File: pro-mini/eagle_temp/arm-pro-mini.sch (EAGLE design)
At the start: 61 parts, among them J1 MICRO USB, J2 SWD HEADER, Q1 12Mhz, T1 MMBT3906, U1 PRTR5V0U2X, U2 MIC5225-3.3v, U3 LPC11U35FHI33/501, U4 BAS40-05

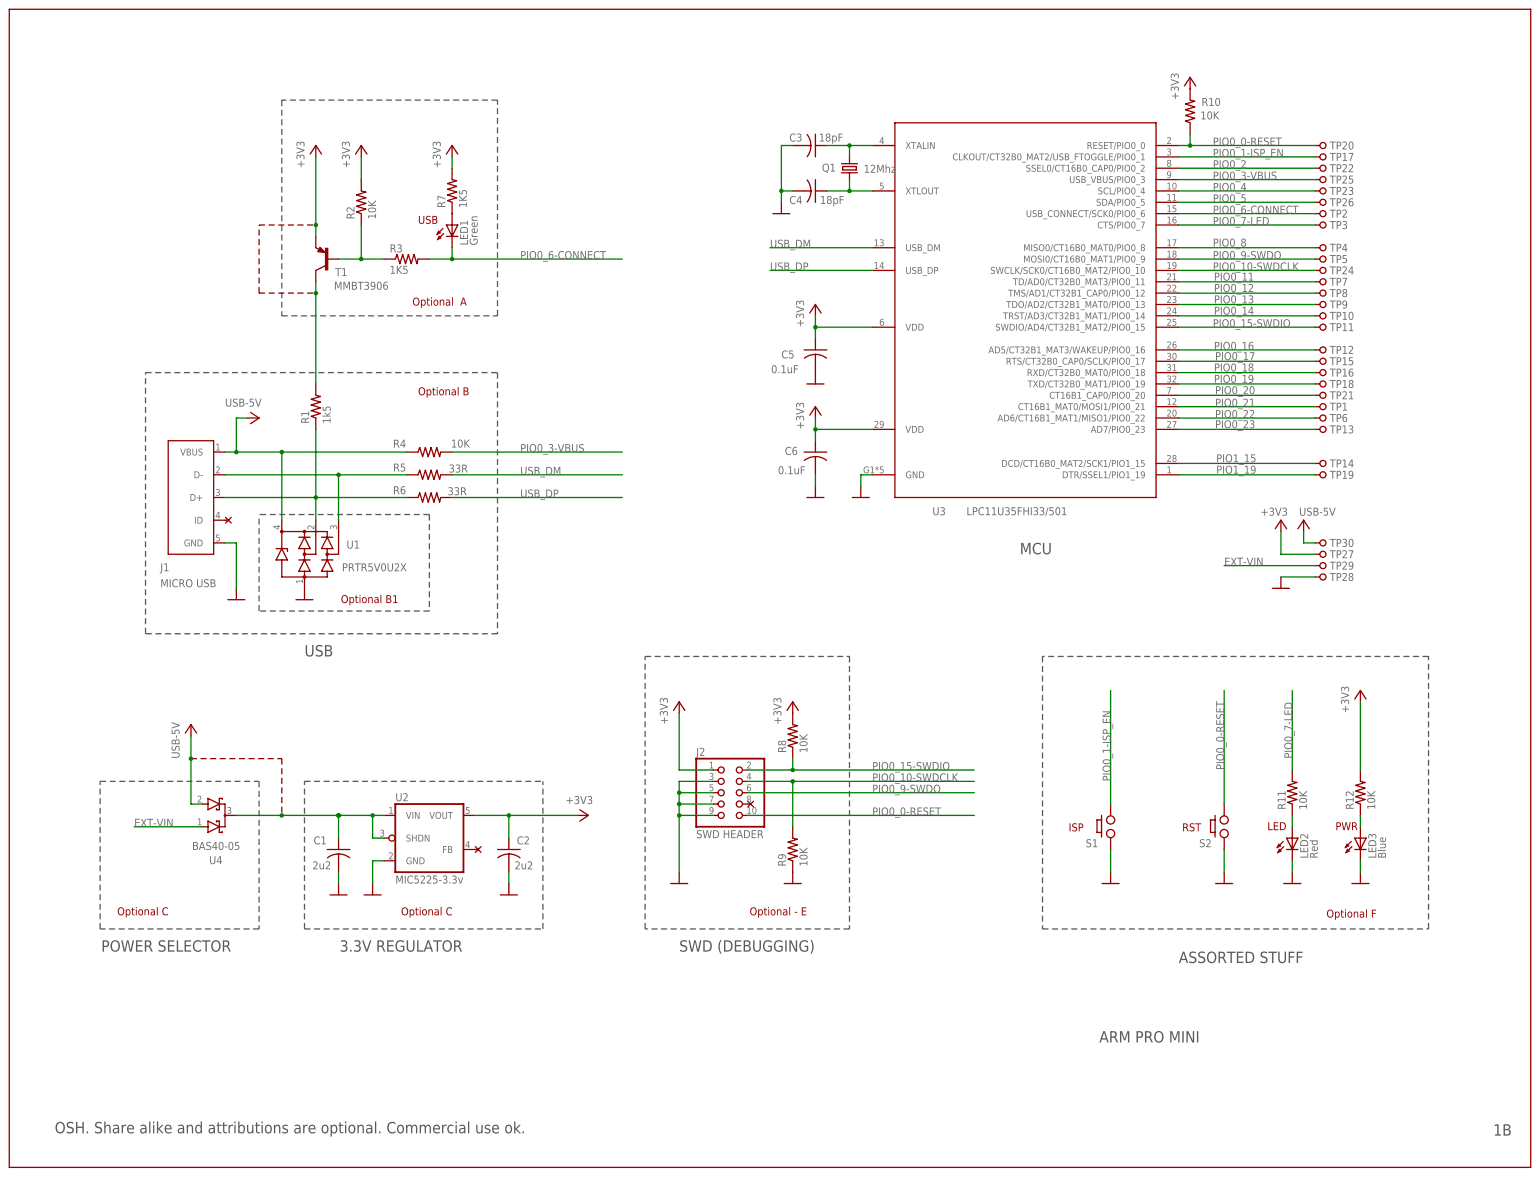
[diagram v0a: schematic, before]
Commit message: Work in progress. Layout auto routs 100%. Requires net list and footprints verification.
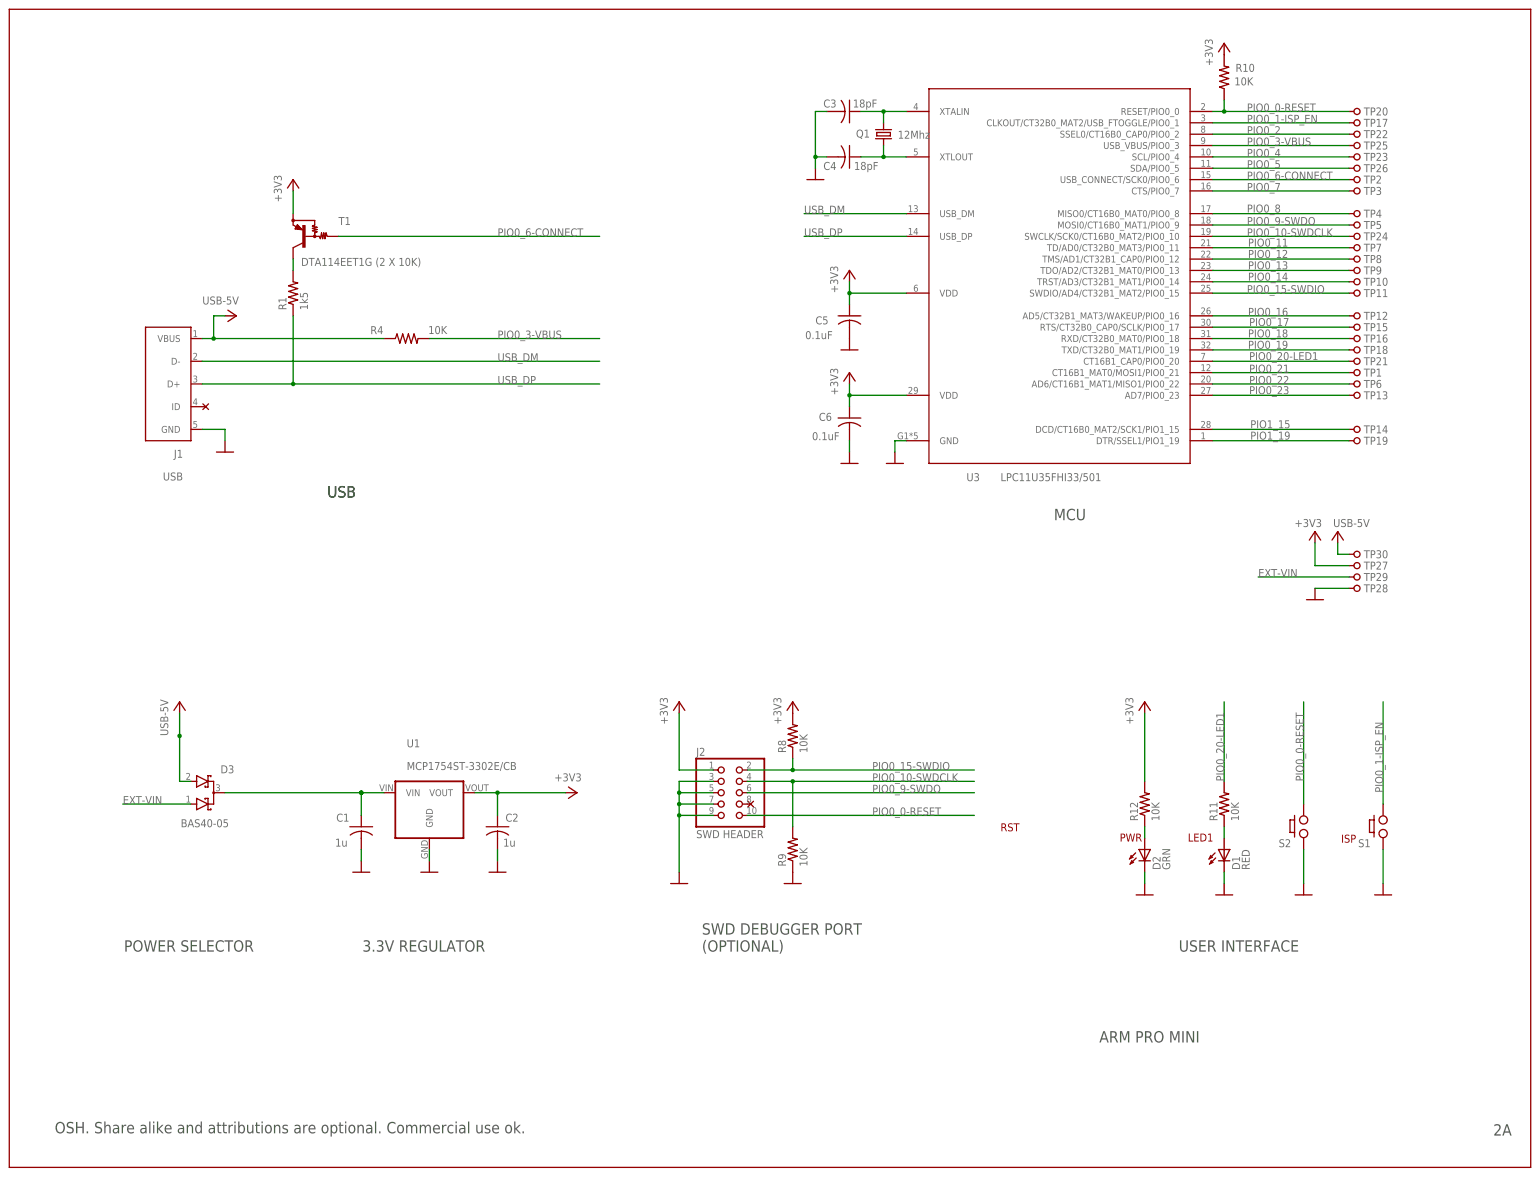
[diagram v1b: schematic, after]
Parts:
- removed LED1: Green, arm-pro-mini:LEDCHIP-LED0603
- removed LED2: Red, arm-pro-mini:LEDCHIP-LED0603
- removed LED3: Blue, arm-pro-mini:LEDCHIP-LED0603
- removed R2: 10K, arm-pro-mini:R-US_R0402
- removed R3, R7: 1K5, arm-pro-mini:R-US_R0402
- removed R5, R6: 33R, arm-pro-mini:R-US_R0402
- removed U2: MIC5225-3.3v, arm-pro-mini:TC1015
- removed U4: BAS40-05, arm-pro-mini:BAS40-05
- added D1: RED, arm-pro-mini:LED
- added D2: GRN, arm-pro-mini:LED
- added D3: BAS40-05, arm-pro-mini:BAS40-05
- C1, C2: value 2u2 -> 1u
- J1: value MICRO USB -> USB
- T1: value MMBT3906 -> DTA114EET1G (2 X 10K); device arm-pro-mini:BC857B-PNP-SOT23-BEC -> arm-pro-mini:PNP_RESISTORS
- U1: value PRTR5V0U2X -> MCP1754ST-3302E/CB; device arm-pro-mini:PRTR5V0U2X -> arm-pro-mini:LDO
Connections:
- removed net N$4: R2.1, R3.1, T1.B
- removed net N$7: LED1.A, R7.1
- removed net N$8: J1.D+, R1.1, R6.1, U1.IO1
- removed net N$9: J1.D-, R5.1, U1.IO2
- removed net PIO0_20: TP21.1, U3.CT16B1_CAP0/PIO0_20
- removed net PIO0_7-LED: R11.2, TP3.1, U3.CTS/PIO0_7
- new net PIO0_20-LED1: R11.2, TP21.1, U3.CT16B1_CAP0/PIO0_20
- new net PIO0_7: TP3.1, U3.CTS/PIO0_7
- net +3V3: now also U1.VOUT; no longer R2.2, R7.2, U2.VOUT
- net EXT-VIN: now also D3.A1; no longer U4.A1
- net GND: now also D1.C, D2.C; no longer LED2.C, LED3.C, U2.GND
- net N$10: now also D3.C, U1.VIN; no longer U2.SHDN, U2.VIN, U4.C
- net N$2: now also D2.A; no longer LED3.A
- net N$6: now also D1.A; no longer LED2.A
- net PIO0_6-CONNECT: now also T1.B; no longer LED1.C, R3.2
- net USB-5V: now also D3.A2; no longer U1.VCC, U4.A2
- net USB_DM: now also J1.D-; no longer R5.2
- net USB_DP: now also J1.D+, R1.1; no longer R6.2
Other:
- note added: "2A"
- note added: "LED1"
- note added: "SWD DEBUGGER PORT (OPTIONAL)"
- note added: "USER INTERFACE"
- note removed: "1B"
- note removed: "ASSORTED STUFF"
- note removed: "LED"
- note removed: "Optional - E"
- note removed: "Optional A"
- note removed: "Optional B"
- note removed: "Optional B1"
- note removed: "Optional C"
- note removed: "Optional F"
- note removed: "SWD (DEBUGGING)"
- moved on the sheet: C1, C2, C3, C4, C5, C6, J1, Q1, R1, R10, R11, R12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

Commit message: Ready for final auto routing.
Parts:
- removed R8: 10K, arm-pro-mini:R-US_R0402
- added R2: 10K, arm-pro-mini:R-US_R0402
- TP1: device arm-pro-mini:PINHD-1X1SQUARE -> arm-pro-mini:PINHD-1X1
- renumbered R10 to R5, R11 to R7, R12 to R6, R9 to R3
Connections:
- net +3V3: now also R4.2; no longer R8.2
- net PIO0_15-SWDIO: now also R4.1; no longer R8.1
- net PIO0_3-VBUS: now also R2.2; no longer R4.2
- net USB-5V: now also R2.1; no longer R4.1
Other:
- moved on the sheet: J1, R4
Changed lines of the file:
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@@
 <part name="+3V6" library="arm-pro-mini" deviceset="+3V3" device=""/>
 <part name="GND12" library="arm-pro-mini" deviceset="GND" device=""/>
-<part name="R8" library="arm-pro-mini" deviceset="R-US_" device="R0402" value="10K"/>
-<part name="R9" library="arm-pro-mini" deviceset="R-US_" device="R0402" value="10K"/>
+<part name="R4" library="arm-pro-mini" deviceset="R-US_" device="R0402" value="10K"/>
+<part name="R3" library="arm-pro-mini" deviceset="R-US_" device="R0402" value="10K"/>
 <part name="GND13" library="arm-pro-mini" deviceset="GND" device=""/>
 <part name="+3V7" library="arm-pro-mini" deviceset="+3V3" device=""/>
-<part name="R10" library="arm-pro-mini" deviceset="R-US_" device="R0402" value="10K"/>
+<part name="R5" library="arm-pro-mini" deviceset="R-US_" device="R0402" value="10K"/>
 <part name="+3V8" library="arm-pro-mini" deviceset="+3V3" device=""/>
 <part name="S2" library="arm-pro-mini" deviceset="PUSH_BUTTON" device=""/>
 <part name="GND14" library="arm-pro-mini" deviceset="GND" device=""/>
-<part name="R4" library="arm-pro-mini" deviceset="R-US_" device="R0402" value="10K"/>
+<part name="R2" library="arm-pro-mini" deviceset="R-US_" device="R0402" value="10K"/>
 <part name="+3V9" library="arm-pro-mini" deviceset="+3V3" device=""/>
-<part name="R12" library="arm-pro-mini" deviceset="R-US_" device="R0402" value="10K"/>
+<part name="R6" library="arm-pro-mini" deviceset="R-US_" device="R0402" value="10K"/>
 <part name="GND5" library="arm-pro-mini" deviceset="GND" device=""/>
-<part name="R11" library="arm-pro-mini" deviceset="R-US_" device="R0402" value="10K"/>
+<part name="R7" library="arm-pro-mini" deviceset="R-US_" device="R0402" value="10K"/>
 <part name="GND6" library="arm-pro-mini" deviceset="GND" device=""/>
 <part name="+3V4" library="arm-pro-mini" deviceset="+3V3" device=""/>
@@
 <part name="TP18" library="arm-pro-mini" deviceset="PINHD-1X1" device="" value="HDR1"/>
 <part name="TP21" library="arm-pro-mini" deviceset="PINHD-1X1" device="" value="HDR1"/>
-<part name="TP1" library="arm-pro-mini" deviceset="PINHD-1X1" device="SQUARE" value="HDR1"/>
+<part name="TP1" library="arm-pro-mini" deviceset="PINHD-1X1" device="" value="HDR1"/>
 <part name="TP6" library="arm-pro-mini" deviceset="PINHD-1X1" device="" value="HDR1"/>
 <part name="TP13" library="arm-pro-mini" deviceset="PINHD-1X1" device="" value="HDR1"/>
@@
 <instance part="+3V6" gate="G$1" x="149.86" y="104.14"/>
 <instance part="GND12" gate="1" x="149.86" y="63.5"/>
-<instance part="R8" gate="G$1" x="175.26" y="96.52" rot="R90"/>
-<instance part="R9" gate="G$1" x="175.26" y="71.12" rot="R90"/>
+<instance part="R4" gate="G$1" x="175.26" y="96.52" rot="R90"/>
+<instance part="R3" gate="G$1" x="175.26" y="71.12" rot="R90"/>
 <instance part="GND13" gate="1" x="175.26" y="63.5"/>
 <instance part="+3V7" gate="G$1" x="175.26" y="104.14"/>
-<instance part="R10" gate="G$1" x="271.78" y="243.84" smashed="yes" rot="R90">
+<instance part="R5" gate="G$1" x="271.78" y="243.84" smashed="yes" rot="R90">
 <attribute name="NAME" x="274.32" y="245.0846" size="1.778" layer="95"/>
 <attribute name="VALUE" x="274.066" y="242.062" size="1.778" layer="96"/>
@@
 </instance>
 <instance part="GND14" gate="1" x="289.56" y="60.96"/>
-<instance part="R4" gate="G$1" x="88.9" y="185.42" smashed="yes">
+<instance part="R2" gate="G$1" x="88.9" y="185.42" smashed="yes">
 <attribute name="NAME" x="80.772" y="186.4106" size="1.778" layer="95"/>
 <attribute name="VALUE" x="93.726" y="186.436" size="1.778" layer="96"/>
 </instance>
 <instance part="+3V9" gate="G$1" x="63.5" y="220.98"/>
-<instance part="R12" gate="G$1" x="254" y="81.28" rot="R90"/>
+<instance part="R6" gate="G$1" x="254" y="81.28" rot="R90"/>
 <instance part="GND5" gate="1" x="254" y="60.96"/>
-<instance part="R11" gate="G$1" x="271.78" y="81.28" rot="R90"/>
+<instance part="R7" gate="G$1" x="271.78" y="81.28" rot="R90"/>
 <instance part="GND6" gate="1" x="271.78" y="60.96"/>
 <instance part="+3V4" gate="G$1" x="254" y="104.14"/>
@@
 </segment>
 <segment>
-<pinref part="R9" gate="G$1" pin="1"/>
+<pinref part="R3" gate="G$1" pin="1"/>
 <pinref part="GND13" gate="1" pin="GND"/>
 </segment>
@@
 </segment>
 <segment>
-<pinref part="R8" gate="G$1" pin="2"/>
+<pinref part="R4" gate="G$1" pin="2"/>
 <pinref part="+3V7" gate="G$1" pin="+3V3"/>
 </segment>
 <segment>
-<pinref part="R10" gate="G$1" pin="2"/>
+<pinref part="R5" gate="G$1" pin="2"/>
 <pinref part="+3V8" gate="G$1" pin="+3V3"/>
 </segment>
 <segment>
 <pinref part="+3V4" gate="G$1" pin="+3V3"/>
-<pinref part="R12" gate="G$1" pin="2"/>
+<pinref part="R6" gate="G$1" pin="2"/>
 <wire x1="254" y1="101.6" x2="254" y2="86.36" width="0.1524" layer="91"/>
 </segment>
@@
 </segment>
 <segment>
-<pinref part="R11" gate="G$1" pin="2"/>
+<pinref part="R7" gate="G$1" pin="2"/>
 <wire x1="271.78" y1="86.36" x2="271.78" y2="104.14" width="0.1524" layer="91"/>
 <label x="271.78" y="86.36" size="1.778" layer="95" rot="R90"/>
@@
 </segment>
 <segment>
-<pinref part="R4" gate="G$1" pin="2"/>
+<pinref part="R2" gate="G$1" pin="2"/>
 <wire x1="93.98" y1="185.42" x2="132.08" y2="185.42" width="0.1524" layer="91"/>
 <label x="109.22" y="185.42" size="1.778" layer="95"/>
@@
 <junction x="45.72" y="185.42"/>
 <pinref part="P+4" gate="VCC" pin="USB-5V"/>
-<pinref part="R4" gate="G$1" pin="1"/>
+<pinref part="R2" gate="G$1" pin="1"/>
 <wire x1="45.72" y1="185.42" x2="83.82" y2="185.42" width="0.1524" layer="91"/>
 <pinref part="J1" gate="G$1" pin="VBUS"/>
@@
 <wire x1="269.24" y1="236.22" x2="271.78" y2="236.22" width="0.1524" layer="91"/>
 <label x="276.86" y="236.22" size="1.778" layer="95"/>
-<pinref part="R10" gate="G$1" pin="1"/>
+<pinref part="R5" gate="G$1" pin="1"/>
 <wire x1="271.78" y1="236.22" x2="299.72" y2="236.22" width="0.1524" layer="91"/>
 <wire x1="271.78" y1="238.76" x2="271.78" y2="236.22" width="0.1524" layer="91"/>
@@
 <pinref part="J2" gate="A" pin="4"/>
 <wire x1="165.1" y1="86.36" x2="175.26" y2="86.36" width="0.1524" layer="91"/>
-<pinref part="R9" gate="G$1" pin="2"/>
+<pinref part="R3" gate="G$1" pin="2"/>
 <wire x1="175.26" y1="86.36" x2="215.9" y2="86.36" width="0.1524" layer="91"/>
 <wire x1="175.26" y1="86.36" x2="175.26" y2="76.2" width="0.1524" layer="91"/>
@@
 <pinref part="J2" gate="A" pin="2"/>
 <wire x1="165.1" y1="88.9" x2="175.26" y2="88.9" width="0.1524" layer="91"/>
-<pinref part="R8" gate="G$1" pin="1"/>
+<pinref part="R4" gate="G$1" pin="1"/>
 <wire x1="175.26" y1="88.9" x2="215.9" y2="88.9" width="0.1524" layer="91"/>
 <wire x1="175.26" y1="91.44" x2="175.26" y2="88.9" width="0.1524" layer="91"/>
@@
 <net name="N$2" class="0">
 <segment>
-<pinref part="R12" gate="G$1" pin="1"/>
+<pinref part="R6" gate="G$1" pin="1"/>
 <wire x1="254" y1="73.66" x2="254" y2="76.2" width="0.1524" layer="91"/>
 <pinref part="D2" gate="G$1" pin="A"/>
@@
 <net name="N$6" class="0">
 <segment>
-<pinref part="R11" gate="G$1" pin="1"/>
+<pinref part="R7" gate="G$1" pin="1"/>
 <wire x1="271.78" y1="76.2" x2="271.78" y2="73.66" width="0.1524" layer="91"/>
 <pinref part="D1" gate="G$1" pin="A"/>

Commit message: Added esd protection
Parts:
- added U2: NUF2042XV6T1G, arm-pro-mini:USB_FILTER
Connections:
- new net N$4: J1.D-, U2.DMI
- new net N$7: J1.D+, R1.1, U2.DPI
- net GND: now also U2.GND
- net USB-5V: now also U2.VBUS
- net USB_DM: now also U2.DMO; no longer J1.D-
- net USB_DP: now also U2.DPO; no longer J1.D+, R1.1
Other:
- note added: "2C"
- note removed: "2A"
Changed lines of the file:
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@@
 <part name="U1" library="arm-pro-mini" deviceset="LDO" device="" value="MCP1754ST-3302E/CB"/>
 <part name="J1" library="arm-pro-mini" deviceset="USB" device=""/>
+<part name="U2" library="arm-pro-mini" deviceset="USB_FILTER" device="" value="NUF2042XV6T1G"/>
 </parts>
 <sheets>
@@
 <wire x1="0" y1="0" x2="0" y2="259.08" width="0.1524" layer="94"/>
 <text x="233.68" y="144.78" size="2.54" layer="97">MCU</text>
-<text x="331.978" y="7.112" size="2.54" layer="97">2A</text>
+<text x="331.978" y="7.112" size="2.54" layer="97">2C</text>
 <text x="78.994" y="48.26" size="2.54" layer="97">3.3V REGULATOR</text>
 <text x="71.12" y="149.86" size="2.54" layer="97">USB</text>
@@
 </instance>
 <instance part="J1" gate="G$1" x="35.56" y="170.18"/>
+<instance part="U2" gate="G$1" x="88.9" y="167.64"/>
 </instances>
 <busses>
@@
 <wire x1="48.26" y1="165.1" x2="48.26" y2="162.56" width="0.1524" layer="91"/>
 <pinref part="J1" gate="G$1" pin="GND"/>
+<pinref part="U2" gate="G$1" pin="GND"/>
+<wire x1="48.26" y1="165.1" x2="78.74" y2="165.1" width="0.1524" layer="91"/>
+<junction x="48.26" y="165.1"/>
 </segment>
 <segment>
@@
 <pinref part="P+4" gate="VCC" pin="USB-5V"/>
 <pinref part="R2" gate="G$1" pin="1"/>
-<wire x1="45.72" y1="185.42" x2="83.82" y2="185.42" width="0.1524" layer="91"/>
+<wire x1="45.72" y1="185.42" x2="73.66" y2="185.42" width="0.1524" layer="91"/>
 <pinref part="J1" gate="G$1" pin="VBUS"/>
+<pinref part="U2" gate="G$1" pin="VBUS"/>
+<wire x1="73.66" y1="185.42" x2="83.82" y2="185.42" width="0.1524" layer="91"/>
+<wire x1="78.74" y1="172.72" x2="73.66" y2="172.72" width="0.1524" layer="91"/>
+<wire x1="73.66" y1="172.72" x2="73.66" y2="185.42" width="0.1524" layer="91"/>
+<junction x="73.66" y="185.42"/>
 </segment>
 <segment>
 <pinref part="D3" gate="G$1" pin="A2"/>
 <wire x1="40.64" y1="86.36" x2="38.1" y2="86.36" width="0.1524" layer="91"/>
-<wire x1="38.1" y1="86.36" x2="38.1" y2="96.52" width="0.1524" layer="91"/>
+<wire x1="38.1" y1="86.36" x2="38.1" y2="101.6" width="0.1524" layer="91"/>
 <pinref part="P+1" gate="VCC" pin="USB-5V"/>
-<junction x="38.1" y="96.52"/>
-<wire x1="38.1" y1="96.52" x2="38.1" y2="101.6" width="0.1524" layer="91"/>
 </segment>
 <segment>
@@
 <net name="USB_DM" class="2">
 <segment>
-<wire x1="43.18" y1="180.34" x2="132.08" y2="180.34" width="0.1524" layer="91"/>
-<label x="109.22" y="180.34" size="1.778" layer="95"/>
-<pinref part="J1" gate="G$1" pin="D-"/>
+<wire x1="99.06" y1="172.72" x2="132.08" y2="172.72" width="0.1524" layer="91"/>
+<label x="109.22" y="172.72" size="1.778" layer="95"/>
+<pinref part="U2" gate="G$1" pin="DMO"/>
 </segment>
 <segment>
@@
 <net name="USB_DP" class="2">
 <segment>
-<wire x1="63.5" y1="190.5" x2="63.5" y2="175.26" width="0.1524" layer="91"/>
-<wire x1="63.5" y1="175.26" x2="132.08" y2="175.26" width="0.1524" layer="91"/>
-<label x="109.22" y="175.26" size="1.778" layer="95"/>
-<pinref part="R1" gate="G$1" pin="1"/>
-<wire x1="43.18" y1="175.26" x2="63.5" y2="175.26" width="0.1524" layer="91"/>
-<junction x="63.5" y="175.26"/>
-<pinref part="J1" gate="G$1" pin="D+"/>
+<wire x1="99.06" y1="165.1" x2="132.08" y2="165.1" width="0.1524" layer="91"/>
+<label x="109.22" y="165.1" size="1.778" layer="95"/>
+<pinref part="U2" gate="G$1" pin="DPO"/>
 </segment>
 <segment>
@@
 </segment>
 </net>
+<net name="N$4" class="2">
+<segment>
+<wire x1="43.18" y1="180.34" x2="68.58" y2="180.34" width="0.1524" layer="91"/>
+<wire x1="68.58" y1="180.34" x2="68.58" y2="170.18" width="0.1524" layer="91"/>
+<wire x1="68.58" y1="170.18" x2="78.74" y2="170.18" width="0.1524" layer="91"/>
+<pinref part="J1" gate="G$1" pin="D-"/>
+<pinref part="U2" gate="G$1" pin="DMI"/>
+</segment>
+</net>
+<net name="N$7" class="2">
+<segment>
+<wire x1="63.5" y1="175.26" x2="63.5" y2="167.64" width="0.1524" layer="91"/>
+<wire x1="63.5" y1="167.64" x2="78.74" y2="167.64" width="0.1524" layer="91"/>
+<pinref part="J1" gate="G$1" pin="D+"/>
+<wire x1="43.18" y1="175.26" x2="63.5" y2="175.26" width="0.1524" layer="91"/>
+<junction x="63.5" y="175.26"/>
+<wire x1="63.5" y1="190.5" x2="63.5" y2="175.26" width="0.1524" layer="91"/>
+<pinref part="R1" gate="G$1" pin="1"/>
+<pinref part="U2" gate="G$1" pin="DPI"/>
+</segment>
+</net>
